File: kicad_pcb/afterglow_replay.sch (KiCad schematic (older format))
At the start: 98 parts, among them J1 Conn_01x02_Male, J2 Serial Monitor, J3 Conn_02x03_Odd_Even, Q1 BC807, Q2 BC807, Q3 BC807, Q4 BC807, Q5 BC807, Q6 BC807, Q7 BC807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

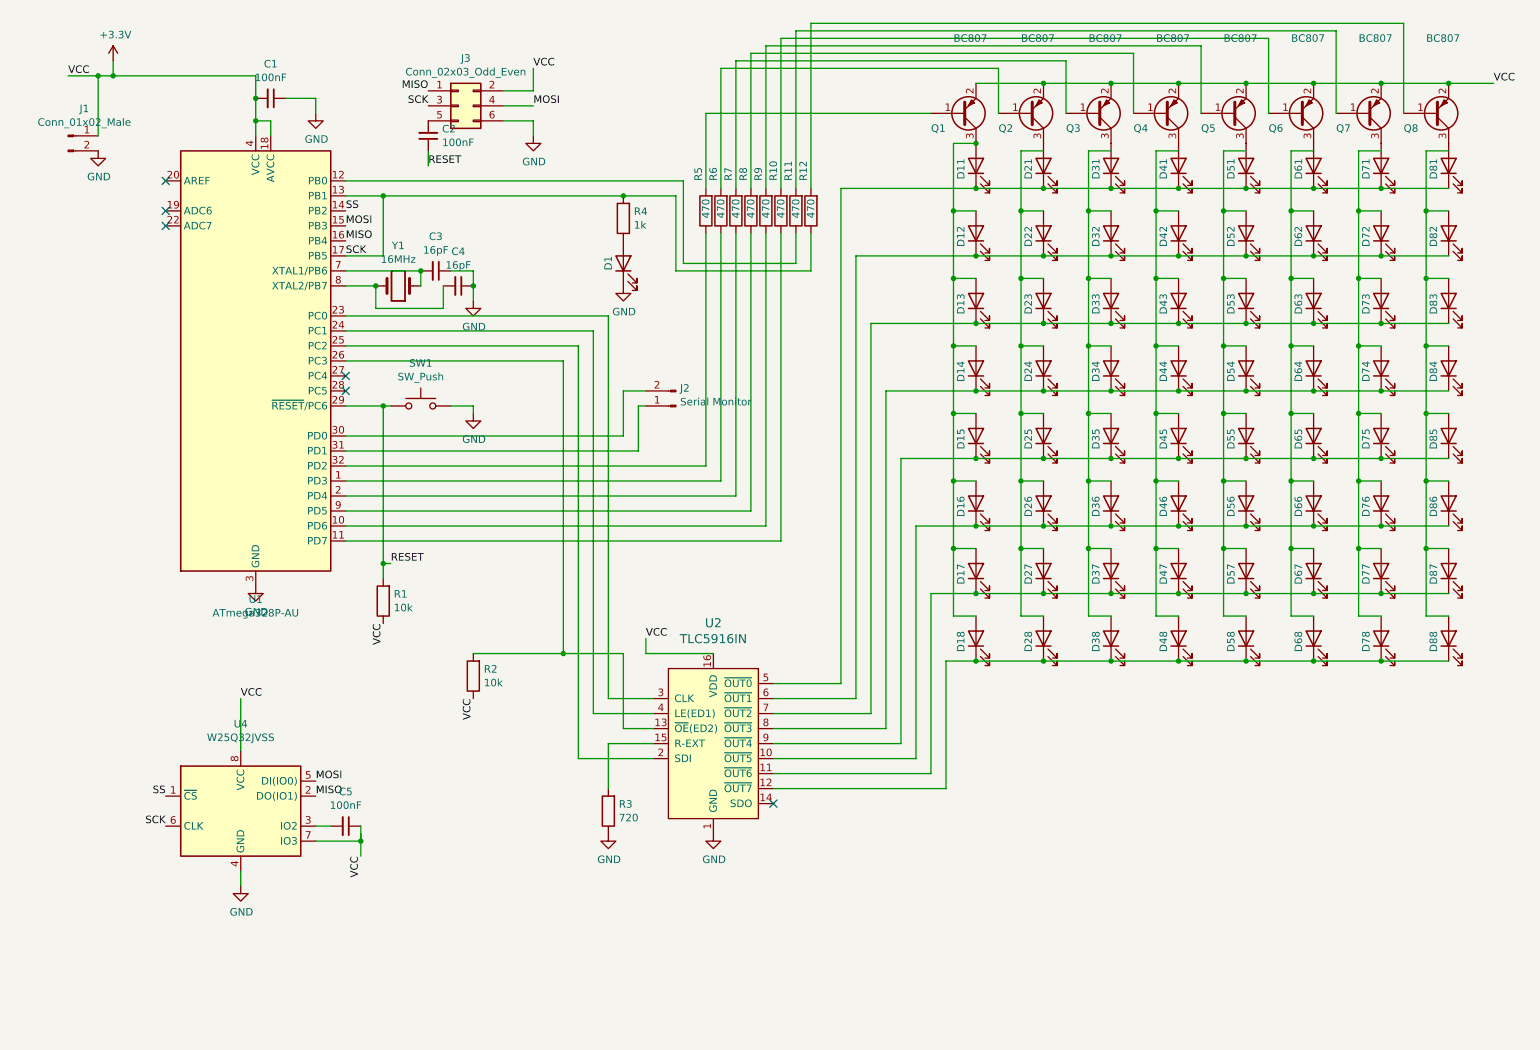
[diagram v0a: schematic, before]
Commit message: Schematic v1.1 fixes the most stupid errors
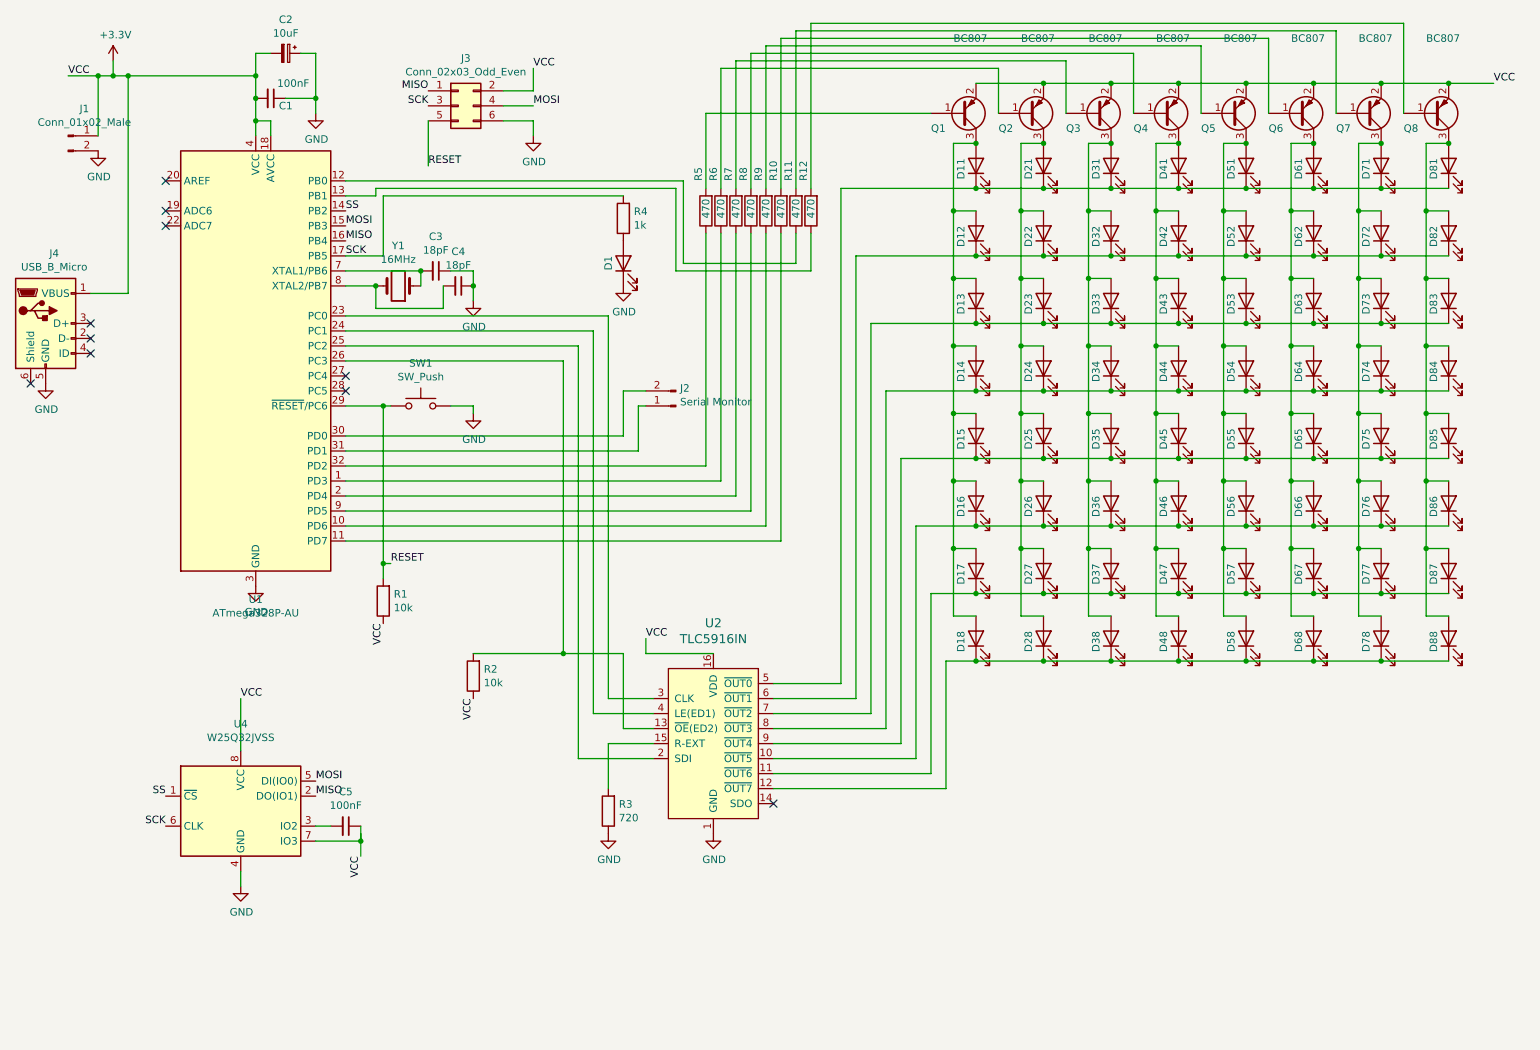
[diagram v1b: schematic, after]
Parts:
- removed C2: 100nF, Capacitors_SMD:C_0805_HandSoldering, symbol Device:C_Small
- added C2: 10uF, Capacitors_THT:CP_Radial_D5.0mm_P2.00mm, symbol Device:CP_Small
- added J4: USB_B_Micro, Connectors_USB:USB_Micro-B_Molex-105017-0001, symbol Connector:USB_B_Micro
- C3, C4: value 16pF -> 18pF
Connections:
- wire segments 321 -> 329
- no-connect marks 6 -> 10
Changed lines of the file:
@@
 Title "Afterglow Replay"
 Date ""
-Rev "1.0"
+Rev "1.1"
 Comp "bitfield labs"
 Comment1 ""
@@
 P 3550 2200
 F 0 "C3" V 3321 2200 50  0000 C CNN
-F 1 "16pF" V 3412 2200 50  0000 C CNN
+F 1 "18pF" V 3412 2200 50  0000 C CNN
 F 2 "Capacitors_SMD:C_0805_HandSoldering" H 3550 2200 50  0001 C CNN
 F 3 "~" H 3550 2200 50  0001 C CNN
@@
 P 3700 2300
 F 0 "C4" V 3471 2300 50  0000 C CNN
-F 1 "16pF" V 3562 2300 50  0000 C CNN
+F 1 "18pF" V 3562 2300 50  0000 C CNN
 F 2 "Capacitors_SMD:C_0805_HandSoldering" H 3700 2300 50  0001 C CNN
 F 3 "~" H 3700 2300 50  0001 C CNN
@@
 U 1 1 5FF21DBC
 P 2450 1050
-F 0 "C1" V 2221 1050 50  0000 C CNN
-F 1 "100nF" V 2312 1050 50  0000 C CNN
+F 0 "C1" V 2500 1150 50  0000 C CNN
+F 1 "100nF" V 2350 1200 50  0000 C CNN
 F 2 "Capacitors_SMD:C_0805_HandSoldering" H 2450 1050 50  0001 C CNN
 F 3 "~" H 2450 1050 50  0001 C CNN
@@
 Connection ~ 1400 900
 Wire Wire Line
-	1400 900  2350 900
+	1400 900  1500 900
 Connection ~ 2350 1050
 Wire Wire Line
@@
 Text Label 3500 1100 2    50   ~ 0
 SCK
-$Comp
-L Device:C_Small C2
-U 1 1 60002BEA
-P 3500 1300
-F 0 "C2" H 3408 1254 50  0000 R CNN
-F 1 "100nF" H 3408 1345 50  0000 R CNN
-F 2 "Capacitors_SMD:C_0805_HandSoldering" H 3500 1300 50  0001 C CNN
-F 3 "~" H 3500 1300 50  0001 C CNN
-	1    3500 1300
-	-1   0    0    1
-$EndComp
 Text Label 3500 1500 0    50   ~ 0
 RESET
@@
 Wire Wire Line
 	3650 3100 3800 3100
-Wire Wire Line
-	3500 1400 3500 1500
 Wire Wire Line
 	2350 1200 2350 1300
@@
 $EndComp
 $Comp
-L Device:LED D71
-U 1 1 5FBB61D2
-P 9850 1500
-F 0 "D71" H 9900 1600 50  0000 R CNN
-F 1 "LED" V 9798 1382 50  0001 R CNN
-F 2 "LEDs:LED_0805_HandSoldering" H 9850 1500 50  0001 C CNN
-F 3 "~" H 9850 1500 50  0001 C CNN
-	1    9850 1500
-	0    -1   -1   0
-$EndComp
-$Comp
 L Device:LED D61
 U 1 1 5FBB6182
@@
 $EndComp
 Wire Wire Line
-	10300 1650 9850 1650
-Wire Wire Line
 	6250 1650 6250 4950
 Wire Wire Line
@@
 Wire Wire Line
 	9400 1650 8950 1650
-Connection ~ 9850 1650
-Wire Wire Line
-	9850 1650 9400 1650
 Wire Wire Line
 	10300 2100 9850 2100
@@
 	9550 600  9550 1150
 Wire Wire Line
-	5150 1700 5150 2200
-Wire Wire Line
 	5150 2200 6050 2200
 Wire Wire Line
 	6050 2200 6050 1950
 Wire Wire Line
-	2950 1700 3200 1700
-Connection ~ 3200 1700
-Wire Wire Line
 	3200 1700 4800 1700
-Connection ~ 4800 1700
-Wire Wire Line
-	4800 1700 5150 1700
 Wire Wire Line
 	6050 1650 6050 550
@@
 	7000 1800 7000 2250
 Wire Wire Line
-	7600 1400 7450 1400
-Wire Wire Line
-	7450 1400 7450 1800
-Wire Wire Line
 	7450 4500 7600 4500
 Wire Wire Line
@@
 	7450 2250 7450 2700
 Wire Wire Line
-	8050 1400 7900 1400
-Wire Wire Line
-	7900 1400 7900 1800
-Wire Wire Line
 	7900 4500 8050 4500
 Connection ~ 7900 4050
@@
 	7450 1800 7450 2250
 Wire Wire Line
-	8500 1400 8350 1400
-Wire Wire Line
-	8350 1400 8350 1800
-Wire Wire Line
 	8350 4500 8500 4500
 Wire Wire Line
@@
 	8350 1800 8350 2250
 Wire Wire Line
-	8950 1400 8800 1400
-Wire Wire Line
-	8800 1400 8800 1800
-Wire Wire Line
 	8800 4500 8950 4500
 Wire Wire Line
@@
 	8800 1800 8800 2250
 Wire Wire Line
-	9400 1400 9250 1400
-Wire Wire Line
 	9250 4500 9400 4500
 Wire Wire Line
@@
 	9250 2250 9250 2700
 Wire Wire Line
-	9250 1400 9250 1800
-Wire Wire Line
 	9400 1800 9250 1800
 Connection ~ 9250 1800
@@
 	9250 1800 9250 2250
 Wire Wire Line
-	9850 1400 9700 1400
-Wire Wire Line
-	9700 1400 9700 1800
-Wire Wire Line
 	9700 4500 9850 4500
 Wire Wire Line
@@
 Wire Wire Line
 	9700 1800 9700 2250
-Wire Wire Line
-	10300 1400 10150 1400
-Wire Wire Line
-	10150 1400 10150 1800
 Wire Wire Line
 	10150 4500 10300 4500
@@
 Connection ~ 7000 1800
 Connection ~ 7150 1350
+Wire Wire Line
+	3500 1200 3500 1500
+Wire Wire Line
+	9850 1650 9400 1650
+Wire Wire Line
+	10300 1650 9850 1650
+Connection ~ 9850 1650
+$Comp
+L Device:LED D71
+U 1 1 5FBB61D2
+P 9850 1500
+F 0 "D71" H 9900 1600 50  0000 R CNN
+F 1 "LED" V 9798 1382 50  0001 R CNN
+F 2 "LEDs:LED_0805_HandSoldering" H 9850 1500 50  0001 C CNN
+F 3 "~" H 9850 1500 50  0001 C CNN
+	1    9850 1500
+	0    -1   -1   0
+$EndComp
+Wire Wire Line
+	10300 1350 10150 1350
+Wire Wire Line
+	10150 1350 10150 1800
+Connection ~ 10300 1350
+Wire Wire Line
+	9700 1350 9700 1800
+Connection ~ 9850 1350
+Wire Wire Line
+	9700 1350 9850 1350
+Wire Wire Line
+	9400 1350 9250 1350
+Wire Wire Line
+	9250 1350 9250 1800
+Connection ~ 9400 1350
+Wire Wire Line
+	8950 1350 8800 1350
+Wire Wire Line
+	8800 1350 8800 1800
+Connection ~ 8950 1350
+Wire Wire Line
+	8500 1350 8350 1350
+Wire Wire Line
+	8350 1350 8350 1800
+Connection ~ 8500 1350
+Wire Wire Line
+	8050 1350 7900 1350
+Wire Wire Line
+	7900 1350 7900 1800
+Connection ~ 8050 1350
+Wire Wire Line
+	7600 1350 7450 1350
+Wire Wire Line
+	7450 1350 7450 1800
+Connection ~ 7600 1350
+Wire Wire Line
+	3150 1700 3150 1650
+Wire Wire Line
+	3150 1650 5150 1650
+Wire Wire Line
+	5150 1650 5150 2200
+Wire Wire Line
+	2950 1700 3150 1700
+Wire Wire Line
+	2750 750  2750 1050
+Connection ~ 2750 1050
+Wire Wire Line
+	2350 750  2350 900
+Connection ~ 2350 900
+Wire Wire Line
+	2350 750  2450 750
+Wire Wire Line
+	2650 750  2750 750
+$Comp
+L Device:CP_Small C2
+U 1 1 5FF8A0D0
+P 2550 750
+F 0 "C2" V 2325 750 50  0000 C CNN
+F 1 "10uF" V 2416 750 50  0000 C CNN
+F 2 "Capacitors_THT:CP_Radial_D5.0mm_P2.00mm" H 2550 750 50  0001 C CNN
+F 3 "~" H 2550 750 50  0001 C CNN
+	1    2550 750
+	0    1    1    0
+$EndComp
+Wire Wire Line
+	1250 2350 1500 2350
+Wire Wire Line
+	1500 2350 1500 900
+Connection ~ 1500 900
+Wire Wire Line
+	1500 900  2350 900
+$Comp
+L power:GND #PWR04
+U 1 1 60044C61
+P 950 2950
+F 0 "#PWR04" H 950 2700 50  0001 C CNN
+F 1 "GND" H 955 2777 50  0000 C CNN
+F 2 "" H 950 2950 50  0001 C CNN
+F 3 "" H 950 2950 50  0001 C CNN
+	1    950  2950
+	1    0    0    -1
+$EndComp
+NoConn ~ 850  2950
+NoConn ~ 1250 2550
+NoConn ~ 1250 2650
+$Comp
+L Connector:USB_B_Micro J4
+U 1 1 600A8C75
+P 950 2550
+F 0 "J4" H 1007 3017 50  0000 C CNN
+F 1 "USB_B_Micro" H 1007 2926 50  0000 C CNN
+F 2 "Connectors_USB:USB_Micro-B_Molex-105017-0001" H 1100 2500 50  0001 C CNN
+F 3 "~" H 1100 2500 50  0001 C CNN
+	1    950  2550
+	1    0    0    -1
+$EndComp
+NoConn ~ 1250 2750
 $EndSCHEMATC

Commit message: PCB v1.2
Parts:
- added J5, J6: Conn_01x02_Male, Pin_Headers:Pin_Header_Straight_1x02_Pitch2.54mm, symbol Connector:Conn_01x02_Male
- C2: footprint Capacitors_THT:CP_Radial_D5.0mm_P2.00mm -> Capacitors_SMD:CP_Elec_4x5.3
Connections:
- net +3V3: now also J5.1 (Pin_1), J6.1 (Pin_1)
- net GND: now also J5.2 (Pin_2), J6.2 (Pin_2)
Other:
- moved on the sheet: C1, C2, C3, C4, C5, D1, D11, D12, D13, D14, D15, D16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
